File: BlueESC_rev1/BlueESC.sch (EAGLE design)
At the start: 69 parts, among them J1 AVR_SPI_PRG_6PTH, Q4 SI7370, Q5 SI7370, Q6 SI7370, Q7 SI7370, Q8 SI7370, Q9 SI7370, U1 ATMEGA168, U2 V_REG_LDOSMD, Y1 RESONATORSMD

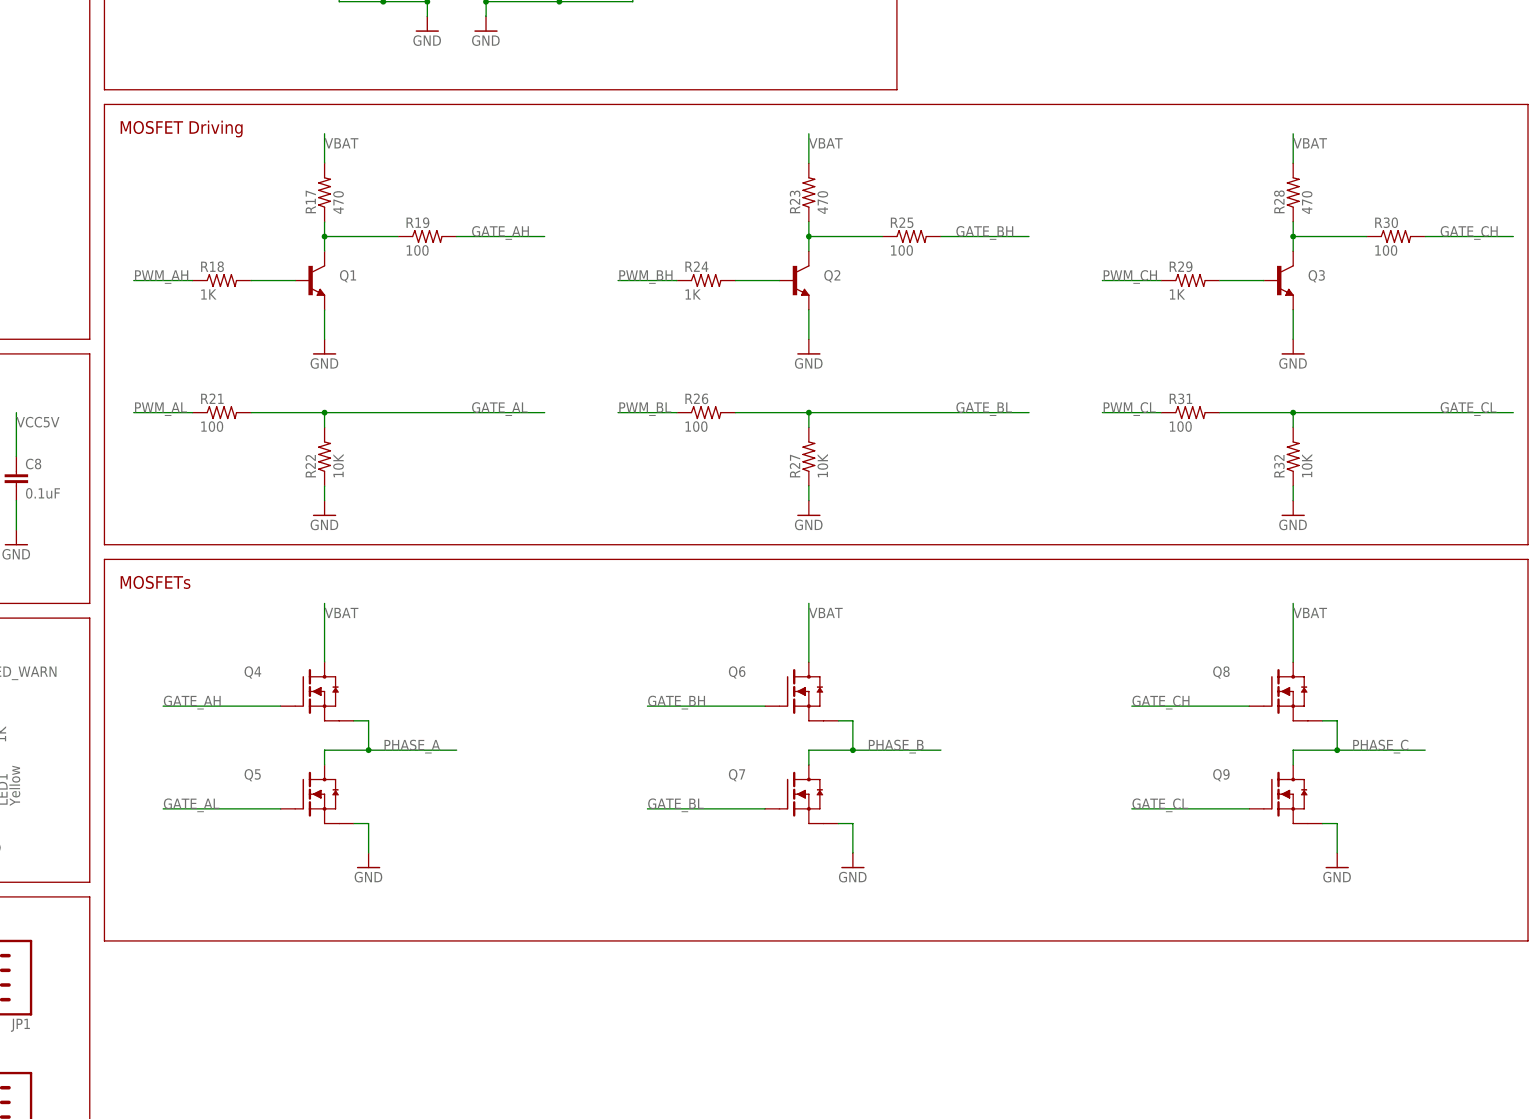
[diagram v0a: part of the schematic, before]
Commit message: Added diodes and capacitors near fets. Need to verify necessary package sizes.
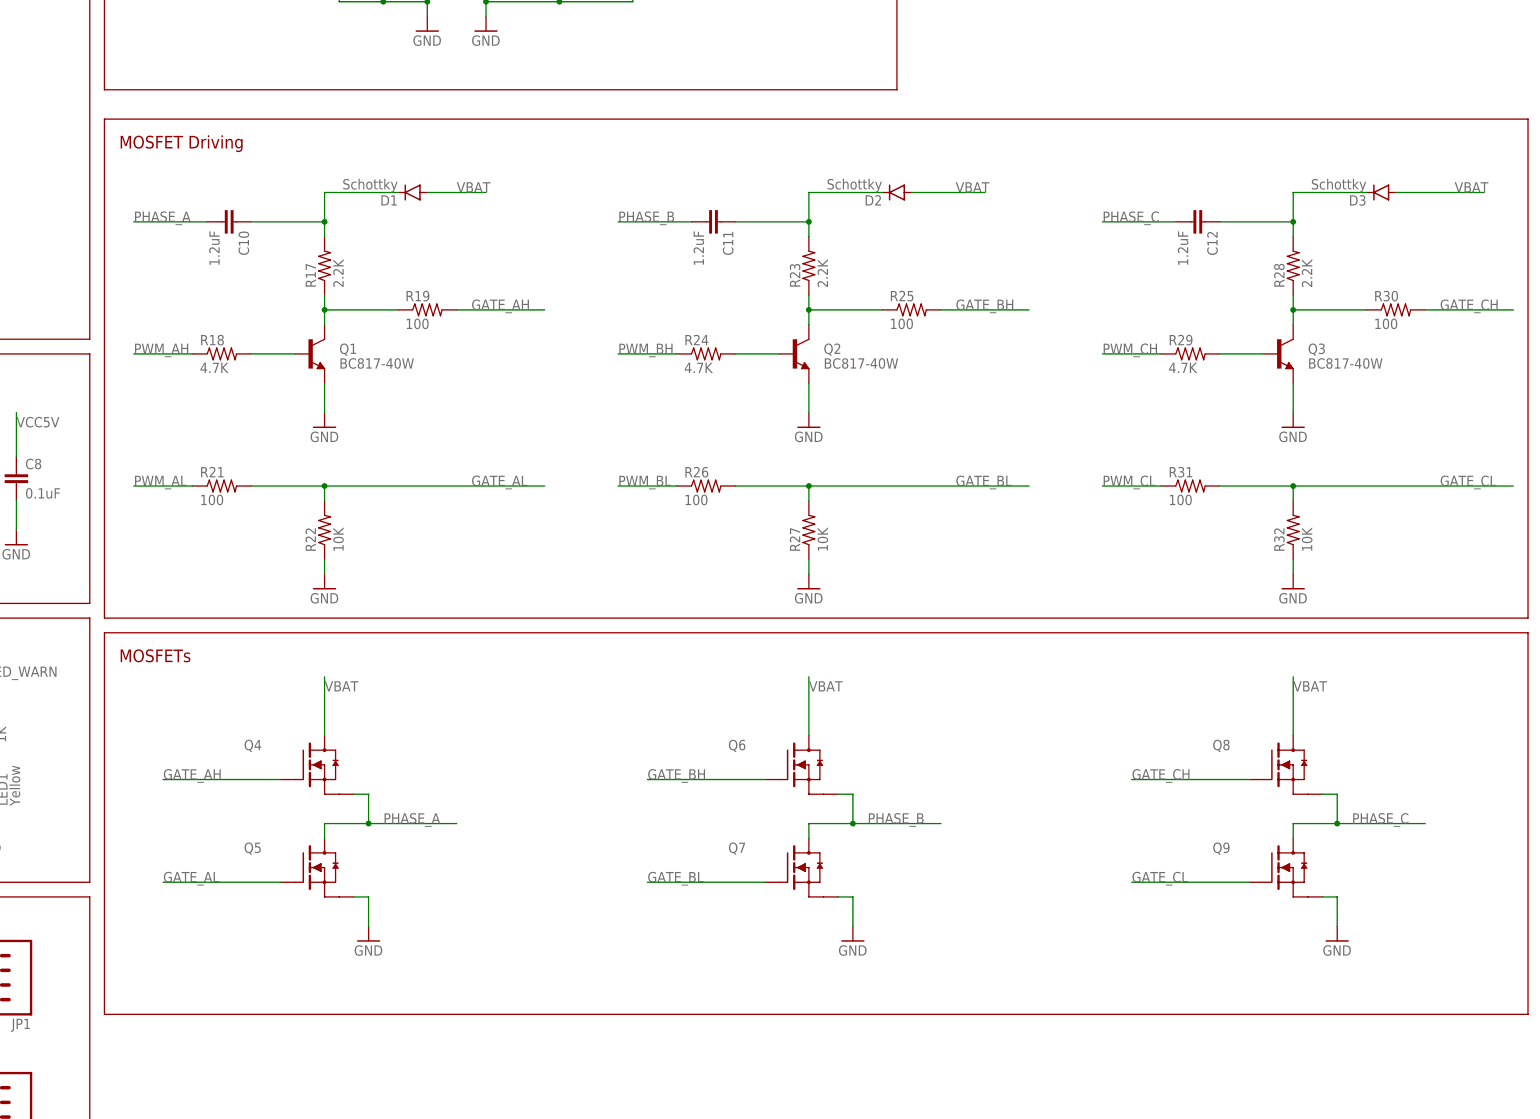
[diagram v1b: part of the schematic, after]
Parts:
- added C10, C11, C12: 1.2uF, SparkFun-Capacitors:CAP0805
- added D1, D2, D3: Schottky, SparkFun-DiscreteSemi:DIODESOD
- Q1, Q2, Q3: value (none) -> BC817-40W
- R17, R23, R28: value 470 -> 2.2K
- R18, R24, R29: value 1K -> 4.7K
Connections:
- new net N$1: C10.1, D1.C, R17.2
- new net N$13: C11.1, D2.C, R23.2
- new net N$15: C12.1, D3.C, R28.2
- net PHASE_A: now also C10.2
- net PHASE_B: now also C11.2
- net PHASE_C: now also C12.2
- net VBAT: now also D1.A, D2.A, D3.A; no longer R17.2, R23.2, R28.2
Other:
- moved on the sheet: Q1, Q2, Q3, Q4, Q5, Q6, Q7, Q8, Q9, R17, R18, R19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

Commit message: Small changes.
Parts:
- Q6: value SI7370 -> SiR158DP
- R1, R2, R3: value 33K -> 3.3K
- R4, R5, R6: value 33K -> 18K
- R7, R8, R9: value 10K -> 3.3K
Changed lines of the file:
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@@
 <parts>
 <part name="U1" library="SparkFun-DigitalIC" deviceset="ATMEGA168" device="" value="ATMEGA168"/>
-<part name="R1" library="SparkFun-Resistors" deviceset="33KOHM1/10W1%(0603)" device="" value="33K"/>
-<part name="R2" library="SparkFun-Resistors" deviceset="33KOHM1/10W1%(0603)" device="" value="33K"/>
-<part name="R3" library="SparkFun-Resistors" deviceset="33KOHM1/10W1%(0603)" device="" value="33K"/>
-<part name="R4" library="SparkFun-Resistors" deviceset="33KOHM1/10W1%(0603)" device="" value="33K"/>
-<part name="R5" library="SparkFun-Resistors" deviceset="33KOHM1/10W1%(0603)" device="" value="33K"/>
-<part name="R6" library="SparkFun-Resistors" deviceset="33KOHM1/10W1%(0603)" device="" value="33K"/>
-<part name="R7" library="SparkFun-Resistors" deviceset="RESISTOR" device="0603" value="10K"/>
-<part name="R8" library="SparkFun-Resistors" deviceset="RESISTOR" device="0603" value="10K"/>
-<part name="R9" library="SparkFun-Resistors" deviceset="RESISTOR" device="0603" value="10K"/>
+<part name="R1" library="SparkFun-Resistors" deviceset="33KOHM1/10W1%(0603)" device="" value="3.3K"/>
+<part name="R2" library="SparkFun-Resistors" deviceset="33KOHM1/10W1%(0603)" device="" value="3.3K"/>
+<part name="R3" library="SparkFun-Resistors" deviceset="33KOHM1/10W1%(0603)" device="" value="3.3K"/>
+<part name="R4" library="SparkFun-Resistors" deviceset="33KOHM1/10W1%(0603)" device="" value="18K"/>
+<part name="R5" library="SparkFun-Resistors" deviceset="33KOHM1/10W1%(0603)" device="" value="18K"/>
+<part name="R6" library="SparkFun-Resistors" deviceset="33KOHM1/10W1%(0603)" device="" value="18K"/>
+<part name="R7" library="SparkFun-Resistors" deviceset="RESISTOR" device="0603" value="3.3K"/>
+<part name="R8" library="SparkFun-Resistors" deviceset="RESISTOR" device="0603" value="3.3K"/>
+<part name="R9" library="SparkFun-Resistors" deviceset="RESISTOR" device="0603" value="3.3K"/>
 <part name="C1" library="SparkFun-Capacitors" deviceset="CAP" device="0603-CAP" value="0.01uF"/>
 <part name="C2" library="SparkFun-Capacitors" deviceset="CAP" device="0603-CAP" value="0.01uF"/>
@@
 <part name="Q5" library="transistor-fet-bobstarr" deviceset="SI7370" device=""/>
 <part name="GND18" library="SparkFun-Aesthetics" deviceset="GND" device=""/>
-<part name="Q6" library="transistor-fet-bobstarr" deviceset="SI7370" device=""/>
+<part name="Q6" library="transistor-fet-bobstarr" deviceset="SI7370" device="" value="SiR158DP"/>
 <part name="Q7" library="transistor-fet-bobstarr" deviceset="SI7370" device=""/>
 <part name="GND19" library="SparkFun-Aesthetics" deviceset="GND" device=""/>

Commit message: Changed value of charge pump capacitors because there are more package sizes available for 1.0uF.
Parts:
- C10, C11, C12: value 1.2uF -> 1uF
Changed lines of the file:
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@@
 <grid distance="0.1" unitdist="inch" unit="inch" style="lines" multiple="1" display="no" altdistance="0.01" altunitdist="inch" altunit="inch"/>
 <layers>
-<layer number="1" name="Top" color="4" fill="1" visible="yes" active="no"/>
-<layer number="16" name="Bottom" color="1" fill="1" visible="yes" active="no"/>
-<layer number="17" name="Pads" color="2" fill="1" visible="yes" active="no"/>
-<layer number="18" name="Vias" color="2" fill="1" visible="yes" active="no"/>
-<layer number="19" name="Unrouted" color="6" fill="1" visible="yes" active="no"/>
-<layer number="20" name="Dimension" color="15" fill="1" visible="yes" active="no"/>
-<layer number="21" name="tPlace" color="7" fill="1" visible="yes" active="no"/>
-<layer number="22" name="bPlace" color="7" fill="1" visible="yes" active="no"/>
-<layer number="23" name="tOrigins" color="15" fill="1" visible="yes" active="no"/>
-<layer number="24" name="bOrigins" color="15" fill="1" visible="yes" active="no"/>
-<layer number="25" name="tNames" color="7" fill="1" visible="yes" active="no"/>
-<layer number="26" name="bNames" color="7" fill="1" visible="yes" active="no"/>
-<layer number="27" name="tValues" color="7" fill="1" visible="yes" active="no"/>
-<layer number="28" name="bValues" color="7" fill="1" visible="yes" active="no"/>
+<layer number="1" name="Top" color="4" fill="1" visible="no" active="no"/>
+<layer number="16" name="Bottom" color="1" fill="1" visible="no" active="no"/>
+<layer number="17" name="Pads" color="2" fill="1" visible="no" active="no"/>
+<layer number="18" name="Vias" color="2" fill="1" visible="no" active="no"/>
+<layer number="19" name="Unrouted" color="6" fill="1" visible="no" active="no"/>
+<layer number="20" name="Dimension" color="15" fill="1" visible="no" active="no"/>
+<layer number="21" name="tPlace" color="7" fill="1" visible="no" active="no"/>
+<layer number="22" name="bPlace" color="7" fill="1" visible="no" active="no"/>
+<layer number="23" name="tOrigins" color="15" fill="1" visible="no" active="no"/>
+<layer number="24" name="bOrigins" color="15" fill="1" visible="no" active="no"/>
+<layer number="25" name="tNames" color="7" fill="1" visible="no" active="no"/>
+<layer number="26" name="bNames" color="7" fill="1" visible="no" active="no"/>
+<layer number="27" name="tValues" color="7" fill="1" visible="no" active="no"/>
+<layer number="28" name="bValues" color="7" fill="1" visible="no" active="no"/>
 <layer number="29" name="tStop" color="7" fill="3" visible="no" active="no"/>
 <layer number="30" name="bStop" color="7" fill="6" visible="no" active="no"/>
@@
 <layer number="35" name="tGlue" color="7" fill="4" visible="no" active="no"/>
 <layer number="36" name="bGlue" color="7" fill="5" visible="no" active="no"/>
-<layer number="37" name="tTest" color="7" fill="1" visible="yes" active="no"/>
-<layer number="38" name="bTest" color="7" fill="1" visible="yes" active="no"/>
+<layer number="37" name="tTest" color="7" fill="1" visible="no" active="no"/>
+<layer number="38" name="bTest" color="7" fill="1" visible="no" active="no"/>
 <layer number="39" name="tKeepout" color="4" fill="11" visible="no" active="no"/>
 <layer number="40" name="bKeepout" color="1" fill="11" visible="no" active="no"/>
@@
 <layer number="44" name="Drills" color="7" fill="1" visible="no" active="no"/>
 <layer number="45" name="Holes" color="7" fill="1" visible="no" active="no"/>
-<layer number="46" name="Milling" color="3" fill="1" visible="yes" active="no"/>
-<layer number="47" name="Measures" color="7" fill="1" visible="yes" active="no"/>
-<layer number="48" name="Document" color="7" fill="1" visible="yes" active="no"/>
-<layer number="49" name="Reference" color="7" fill="1" visible="yes" active="no"/>
-<layer number="50" name="dxf" color="7" fill="1" visible="yes" active="no"/>
-<layer number="51" name="tDocu" color="7" fill="1" visible="yes" active="no"/>
-<layer number="52" name="bDocu" color="7" fill="1" visible="yes" active="no"/>
-<layer number="53" name="tGND_GNDA" color="7" fill="9" visible="yes" active="no"/>
-<layer number="54" name="bGND_GNDA" color="1" fill="9" visible="yes" active="no"/>
-<layer number="56" name="wert" color="7" fill="1" visible="yes" active="no"/>
-<layer number="57" name="tCAD" color="7" fill="1" visible="yes" active="no"/>
+<layer number="46" name="Milling" color="3" fill="1" visible="no" active="no"/>
+<layer number="47" name="Measures" color="7" fill="1" visible="no" active="no"/>
+<layer number="48" name="Document" color="7" fill="1" visible="no" active="no"/>
+<layer number="49" name="Reference" color="7" fill="1" visible="no" active="no"/>
+<layer number="50" name="dxf" color="7" fill="1" visible="no" active="no"/>
+<layer number="51" name="tDocu" color="7" fill="1" visible="no" active="no"/>
+<layer number="52" name="bDocu" color="7" fill="1" visible="no" active="no"/>
+<layer number="53" name="tGND_GNDA" color="7" fill="9" visible="no" active="no"/>
+<layer number="54" name="bGND_GNDA" color="1" fill="9" visible="no" active="no"/>
+<layer number="56" name="wert" color="7" fill="1" visible="no" active="no"/>
+<layer number="57" name="tCAD" color="7" fill="1" visible="no" active="no"/>
 <layer number="91" name="Nets" color="2" fill="1" visible="yes" active="yes"/>
 <layer number="92" name="Busses" color="1" fill="1" visible="yes" active="yes"/>
@@
 <part name="D2" library="SparkFun-DiscreteSemi" deviceset="DIODE" device="SOD" value="Schottky"/>
 <part name="D3" library="SparkFun-DiscreteSemi" deviceset="DIODE" device="SOD" value="Schottky"/>
-<part name="C10" library="SparkFun-Capacitors" deviceset="CAP" device="0805" value="1.2uF"/>
-<part name="C11" library="SparkFun-Capacitors" deviceset="CAP" device="0805" value="1.2uF"/>
-<part name="C12" library="SparkFun-Capacitors" deviceset="CAP" device="0805" value="1.2uF"/>
+<part name="C10" library="SparkFun-Capacitors" deviceset="CAP" device="0805" value="1uF"/>
+<part name="C11" library="SparkFun-Capacitors" deviceset="CAP" device="0805" value="1uF"/>
+<part name="C12" library="SparkFun-Capacitors" deviceset="CAP" device="0805" value="1uF"/>
 </parts>
 <sheets>
